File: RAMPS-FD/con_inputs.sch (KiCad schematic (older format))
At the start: 20 parts, among them K301 X-MIN, K302 X-MAX, K303 Y-MIN, K304 Y-MAX, K305 Z-MIN, K306 Z-MAX, P301 CONN_6, U301 74HC4050

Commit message: RAMPS-FD update
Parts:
- removed R304, R305, R306, R307, R308, R309: 10k, symbol R
- removed U301: 74HC4050, symbol 4050_RMC
- added C304, C305: 100n, symbol C
- added U301: TXS0108, symbol TXS0108
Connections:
- wire segments 76 -> 71
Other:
- moved on the sheet: K301, K302, K303, K304, K305, K306

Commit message: First version of RAMPS-FD, RIB
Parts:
- removed P301: CONN_6, symbol CONN_6
- added C501: 10u, symbol CP1
- added C502, C503, C504, C505: 100nF, symbol C
- added P301: CONN_4X2, symbol CONN_4X2
- added R501: 4k7, symbol R
- added R502, R503, R504, R505: 22, symbol R
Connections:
- net labels added: +V_LOGIC, THERM3, UART_RX, UART_RX_LVC, UART_TX, UART_TX_LVC
- net labels removed: +3.3V
- wire segments 71 -> 97
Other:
- note added: "From \nthermistor"
- note added: "Should use AREF?"
- note added: "To CPU"
- moved on the sheet: C301, C302, C303, R301, R302, R303

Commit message: RAMPS-FD update
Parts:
- removed C304: 100n, symbol C
- removed U301: TXS0108, symbol TXS0108
- added U4: 74LVC07A, symbol 74LVC07A
- C502, C503, C504, C505: value 100nF -> 100n
- R502, R503, R504, R505: value 22 -> 22R
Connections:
- net labels removed: UART_RX, UART_RX_LVC, UART_TX, UART_TX_LVC
- wire segments 97 -> 87

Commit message: Updates to RAMPS-FD
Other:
- note added: "Endstop inputs are 5V tolerant"
- note removed: "Endstops 5V"
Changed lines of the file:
@@
-EESchema Schematic File Version 2  date 19/09/2013 22:01:21
+EESchema Schematic File Version 2
 LIBS:power
 LIBS:device
@@
 LIBS:opendous
 LIBS:RAMPS-FD-cache
-EELAYER 25  0
+EELAYER 27 0
 EELAYER END
-$Descr A4 11700 8267
+$Descr A4 11693 8268
 encoding utf-8
-Sheet 8 8
+Sheet 8 9
 Title "RAMPS-FS RAMPS for Due"
-Date "19 sep 2013"
+Date "22 sep 2013"
 Rev "0.2"
 Comp ""
@@
 F 0 "U4" H 3950 3250 60  0000 C CNN
 F 1 "74LVC07A" H 4500 3250 60  0000 C CNN
+F 2 "" H 4200 3850 60  0001 C CNN
+F 3 "" H 4200 3850 60  0001 C CNN
 	1    4200 3850
 	1    0    0    -1
@@
 F 0 "R504" V 8800 1250 50  0000 C CNN
 F 1 "22R" V 8900 1250 50  0000 C CNN
+F 2 "" H 8900 1250 60  0001 C CNN
+F 3 "" H 8900 1250 60  0001 C CNN
 	1    8900 1250
 	0    -1   -1   0
@@
 F 0 "C504" H 9250 1600 50  0000 L CNN
 F 1 "100n" H 9250 1400 50  0000 L CNN
+F 2 "" H 9200 1500 60  0001 C CNN
+F 3 "" H 9200 1500 60  0001 C CNN
 	1    9200 1500
 	1    0    0    -1
@@
 F 0 "R505" V 8800 2750 50  0000 C CNN
 F 1 "22R" V 8900 2750 50  0000 C CNN
+F 2 "" H 8900 2750 60  0001 C CNN
+F 3 "" H 8900 2750 60  0001 C CNN
 	1    8900 2750
 	0    -1   -1   0
@@
 F 0 "C505" H 9250 3100 50  0000 L CNN
 F 1 "100n" H 9250 2900 50  0000 L CNN
+F 2 "" H 9200 3000 60  0001 C CNN
+F 3 "" H 9200 3000 60  0001 C CNN
 	1    9200 3000
 	1    0    0    -1
@@
 F 0 "C503" H 9050 4650 50  0000 L CNN
 F 1 "100n" H 9050 4450 50  0000 L CNN
+F 2 "" H 9000 4550 60  0001 C CNN
+F 3 "" H 9000 4550 60  0001 C CNN
 	1    9000 4550
 	1    0    0    -1
@@
 F 0 "R503" V 8600 4300 50  0000 C CNN
 F 1 "22R" V 8700 4300 50  0000 C CNN
+F 2 "" H 8700 4300 60  0001 C CNN
+F 3 "" H 8700 4300 60  0001 C CNN
 	1    8700 4300
 	0    -1   -1   0
@@
 F 0 "R502" V 8600 5850 50  0000 C CNN
 F 1 "22R" V 8700 5850 50  0000 C CNN
+F 2 "" H 8700 5850 60  0001 C CNN
+F 3 "" H 8700 5850 60  0001 C CNN
 	1    8700 5850
 	0    -1   -1   0
@@
 F 0 "C502" H 9050 6300 50  0000 L CNN
 F 1 "100n" H 9050 6100 50  0000 L CNN
+F 2 "" H 9000 6200 60  0001 C CNN
+F 3 "" H 9000 6200 60  0001 C CNN
 	1    9000 6200
 	1    0    0    -1
@@
 F 0 "#PWR098" H 9800 5170 30  0001 C CNN
 F 1 "+V_LOGIC" H 9800 5300 30  0000 C CNN
+F 2 "" H 9800 5200 60  0001 C CNN
+F 3 "" H 9800 5200 60  0001 C CNN
 	1    9800 5200
 	1    0    0    -1
@@
 F 0 "#PWR099" H 9800 3670 30  0001 C CNN
 F 1 "+V_LOGIC" H 9800 3800 30  0000 C CNN
+F 2 "" H 9800 3700 60  0001 C CNN
+F 3 "" H 9800 3700 60  0001 C CNN
 	1    9800 3700
 	1    0    0    -1
@@
 F 0 "#PWR0100" H 9800 2120 30  0001 C CNN
 F 1 "+V_LOGIC" H 9800 2250 30  0000 C CNN
+F 2 "" H 9800 2150 60  0001 C CNN
+F 3 "" H 9800 2150 60  0001 C CNN
 	1    9800 2150
 	1    0    0    -1
@@
 F 0 "#PWR0101" H 9800 620 30  0001 C CNN
 F 1 "+V_LOGIC" H 9800 750 30  0000 C CNN
+F 2 "" H 9800 650 60  0001 C CNN
+F 3 "" H 9800 650 60  0001 C CNN
 	1    9800 650
 	1    0    0    -1
@@
 F 0 "#PWR0102" H 4200 2920 30  0001 C CNN
 F 1 "+V_LOGIC" H 4200 3050 30  0000 C CNN
+F 2 "" H 4200 2950 60  0001 C CNN
+F 3 "" H 4200 2950 60  0001 C CNN
 	1    4200 2950
 	1    0    0    -1
@@
 F 0 "#PWR0103" H 4500 1670 30  0001 C CNN
 F 1 "+V_LOGIC" H 4500 1800 30  0000 C CNN
+F 2 "" H 4500 1700 60  0001 C CNN
+F 3 "" H 4500 1700 60  0001 C CNN
 	1    4500 1700
 	1    0    0    -1
@@
 F 0 "R501" V 9880 5550 50  0000 C CNN
 F 1 "4k7" V 9800 5550 50  0000 C CNN
+F 2 "" H 9800 5550 60  0001 C CNN
+F 3 "" H 9800 5550 60  0001 C CNN
 	1    9800 5550
 	1    0    0    -1
@@
 F 0 "C501" H 9850 6300 50  0000 L CNN
 F 1 "10u" H 9850 6100 50  0000 L CNN
+F 2 "" H 9800 6200 60  0001 C CNN
+F 3 "" H 9800 6200 60  0001 C CNN
 	1    9800 6200
 	1    0    0    -1
@@
 F 0 "#PWR0104" H 9800 6600 30  0001 C CNN
 F 1 "GND" H 9800 6530 30  0001 C CNN
+F 2 "" H 9800 6600 60  0001 C CNN
+F 3 "" H 9800 6600 60  0001 C CNN
 	1    9800 6600
 	1    0    0    -1
@@
 F 0 "#PWR0105" H 6250 2800 30  0001 C CNN
 F 1 "GND" H 6250 2730 30  0001 C CNN
+F 2 "" H 6250 2800 60  0001 C CNN
+F 3 "" H 6250 2800 60  0001 C CNN
 	1    6250 2800
 	1    0    0    -1
@@
 F 0 "P301" H 6850 2600 50  0000 C CNN
 F 1 "CONN_4X2" V 6850 2350 40  0000 C CNN
+F 2 "" H 6850 2350 60  0001 C CNN
+F 3 "" H 6850 2350 60  0001 C CNN
 	1    6850 2350
 	1    0    0    -1
@@
 F 0 "#PWR0106" H 4500 2300 30  0001 C CNN
 F 1 "GND" H 4500 2230 30  0001 C CNN
+F 2 "" H 4500 2300 60  0001 C CNN
+F 3 "" H 4500 2300 60  0001 C CNN
 	1    4500 2300
 	1    0    0    -1
@@
 F 0 "C305" H 4550 2100 50  0000 L CNN
 F 1 "100n" H 4550 1900 50  0000 L CNN
+F 2 "" H 4500 2000 60  0001 C CNN
+F 3 "" H 4500 2000 60  0001 C CNN
 	1    4500 2000
 	1    0    0    -1
@@
 F 0 "#PWR0107" H 1650 1590 20  0001 C CNN
 F 1 "+5V" H 1650 1590 30  0000 C CNN
+F 2 "" H 1650 1500 60  0001 C CNN
+F 3 "" H 1650 1500 60  0001 C CNN
 	1    1650 1500
 	1    0    0    -1
@@
 F 0 "#PWR0108" H 4200 4750 30  0001 C CNN
 F 1 "GND" H 4200 4680 30  0001 C CNN
+F 2 "" H 4200 4750 60  0001 C CNN
+F 3 "" H 4200 4750 60  0001 C CNN
 	1    4200 4750
 	1    0    0    -1
@@
 F 0 "#PWR0109" H 9800 4850 30  0001 C CNN
 F 1 "GND" H 9800 4780 30  0001 C CNN
+F 2 "" H 9800 4850 60  0001 C CNN
+F 3 "" H 9800 4850 60  0001 C CNN
 	1    9800 4850
 	1    0    0    -1
@@
 F 0 "C303" H 9850 4650 50  0000 L CNN
 F 1 "10u" H 9850 4450 50  0000 L CNN
+F 2 "" H 9800 4550 60  0001 C CNN
+F 3 "" H 9800 4550 60  0001 C CNN
 	1    9800 4550
 	1    0    0    -1
@@
 F 0 "R303" V 9880 4000 50  0000 C CNN
 F 1 "4k7" V 9800 4000 50  0000 C CNN
+F 2 "" H 9800 4000 60  0001 C CNN
+F 3 "" H 9800 4000 60  0001 C CNN
 	1    9800 4000
 	1    0    0    -1
@@
 F 0 "R302" V 9880 2450 50  0000 C CNN
 F 1 "4k7" V 9800 2450 50  0000 C CNN
+F 2 "" H 9800 2450 60  0001 C CNN
+F 3 "" H 9800 2450 60  0001 C CNN
 	1    9800 2450
 	1    0    0    -1
@@
 F 0 "C302" H 9850 3100 50  0000 L CNN
 F 1 "10u" H 9850 2900 50  0000 L CNN
+F 2 "" H 9800 3000 60  0001 C CNN
+F 3 "" H 9800 3000 60  0001 C CNN
 	1    9800 3000
 	1    0    0    -1
@@
 F 0 "#PWR0110" H 9800 3300 30  0001 C CNN
 F 1 "GND" H 9800 3230 30  0001 C CNN
+F 2 "" H 9800 3300 60  0001 C CNN
+F 3 "" H 9800 3300 60  0001 C CNN
 	1    9800 3300
 	1    0    0    -1
@@
 F 0 "#PWR0111" H 9800 1800 30  0001 C CNN
 F 1 "GND" H 9800 1730 30  0001 C CNN
+F 2 "" H 9800 1800 60  0001 C CNN
+F 3 "" H 9800 1800 60  0001 C CNN
 	1    9800 1800
 	1    0    0    -1
@@
 F 0 "C301" H 9850 1600 50  0000 L CNN
 F 1 "10u" H 9850 1400 50  0000 L CNN
+F 2 "" H 9800 1500 60  0001 C CNN
+F 3 "" H 9800 1500 60  0001 C CNN
 	1    9800 1500
 	1    0    0    -1
@@
 F 0 "R301" V 9880 950 50  0000 C CNN
 F 1 "4k7" V 9800 950 50  0000 C CNN
+F 2 "" H 9800 950 60  0001 C CNN
+F 3 "" H 9800 950 60  0001 C CNN
 	1    9800 950
 	1    0    0    -1
 $EndComp
-Text Notes 1350 2000 2    50   Italic 0
-Endstops 5V
+Text Notes 1850 2150 0    50   Italic 0
+Endstop inputs are 5V tolerant
 Text Notes 1600 6250 2    50   ~ 0
 Endstops
@@
 F 0 "#PWR0112" H 1850 5950 30  0001 C CNN
 F 1 "GND" H 1850 5880 30  0001 C CNN
+F 2 "" H 1850 5950 60  0001 C CNN
+F 3 "" H 1850 5950 60  0001 C CNN
 	1    1850 5950
 	1    0    0    -1
@@
 F 0 "K306" V 1100 2450 50  0000 C CNN
 F 1 "Z-MAX" V 1200 2450 40  0000 C CNN
+F 2 "" H 1150 2450 60  0001 C CNN
+F 3 "" H 1150 2450 60  0001 C CNN
 	1    1150 2450
 	-1   0    0    -1
@@
 F 0 "K305" V 1100 3150 50  0000 C CNN
 F 1 "Z-MIN" V 1200 3150 40  0000 C CNN
+F 2 "" H 1150 3150 60  0001 C CNN
+F 3 "" H 1150 3150 60  0001 C CNN
 	1    1150 3150
 	-1   0    0    -1
@@
 F 0 "K304" V 1100 3750 50  0000 C CNN
 F 1 "Y-MAX" V 1200 3750 40  0000 C CNN
+F 2 "" H 1150 3750 60  0001 C CNN
+F 3 "" H 1150 3750 60  0001 C CNN
 	1    1150 3750
 	-1   0    0    -1
@@
 F 0 "K303" V 1100 4350 50  0000 C CNN
 F 1 "Y-MIN" V 1200 4350 40  0000 C CNN
+F 2 "" H 1150 4350 60  0001 C CNN
+F 3 "" H 1150 4350 60  0001 C CNN
 	1    1150 4350
 	-1   0    0    -1
@@
 F 0 "K302" V 1100 4950 50  0000 C CNN
 F 1 "X-MAX" V 1200 4950 40  0000 C CNN
+F 2 "" H 1150 4950 60  0001 C CNN
+F 3 "" H 1150 4950 60  0001 C CNN
 	1    1150 4950
 	-1   0    0    -1
@@
 F 0 "K301" V 1100 5550 50  0000 C CNN
 F 1 "X-MIN" V 1200 5550 40  0000 C CNN
+F 2 "" H 1150 5550 60  0001 C CNN
+F 3 "" H 1150 5550 60  0001 C CNN
 	1    1150 5550
 	-1   0    0    -1

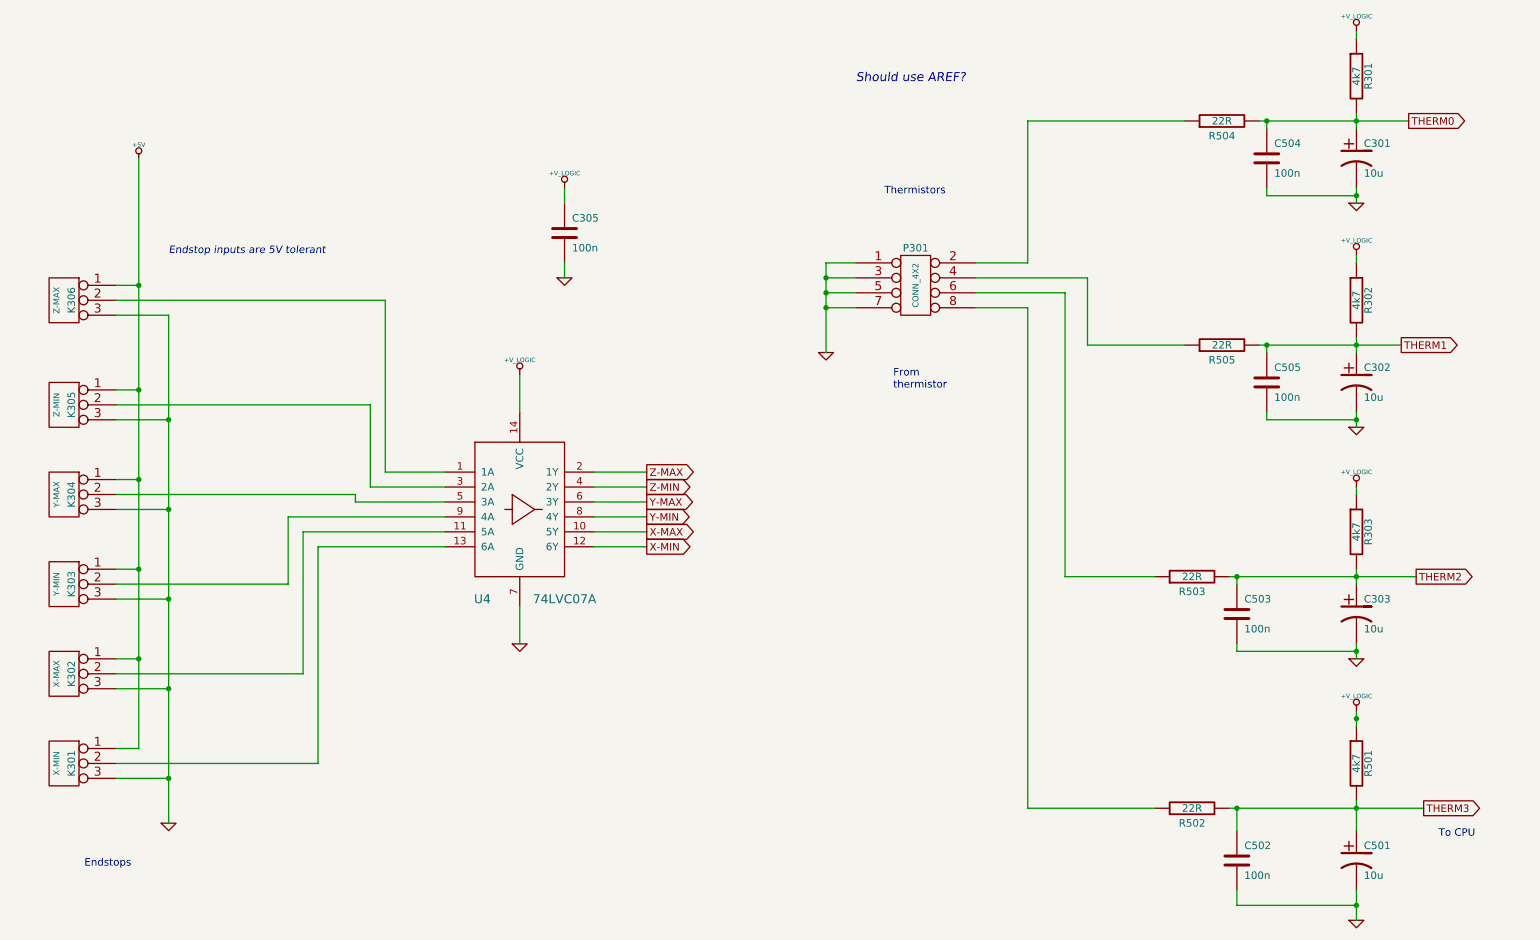
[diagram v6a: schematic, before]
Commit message: RAMPS-FD: update schematic, layout
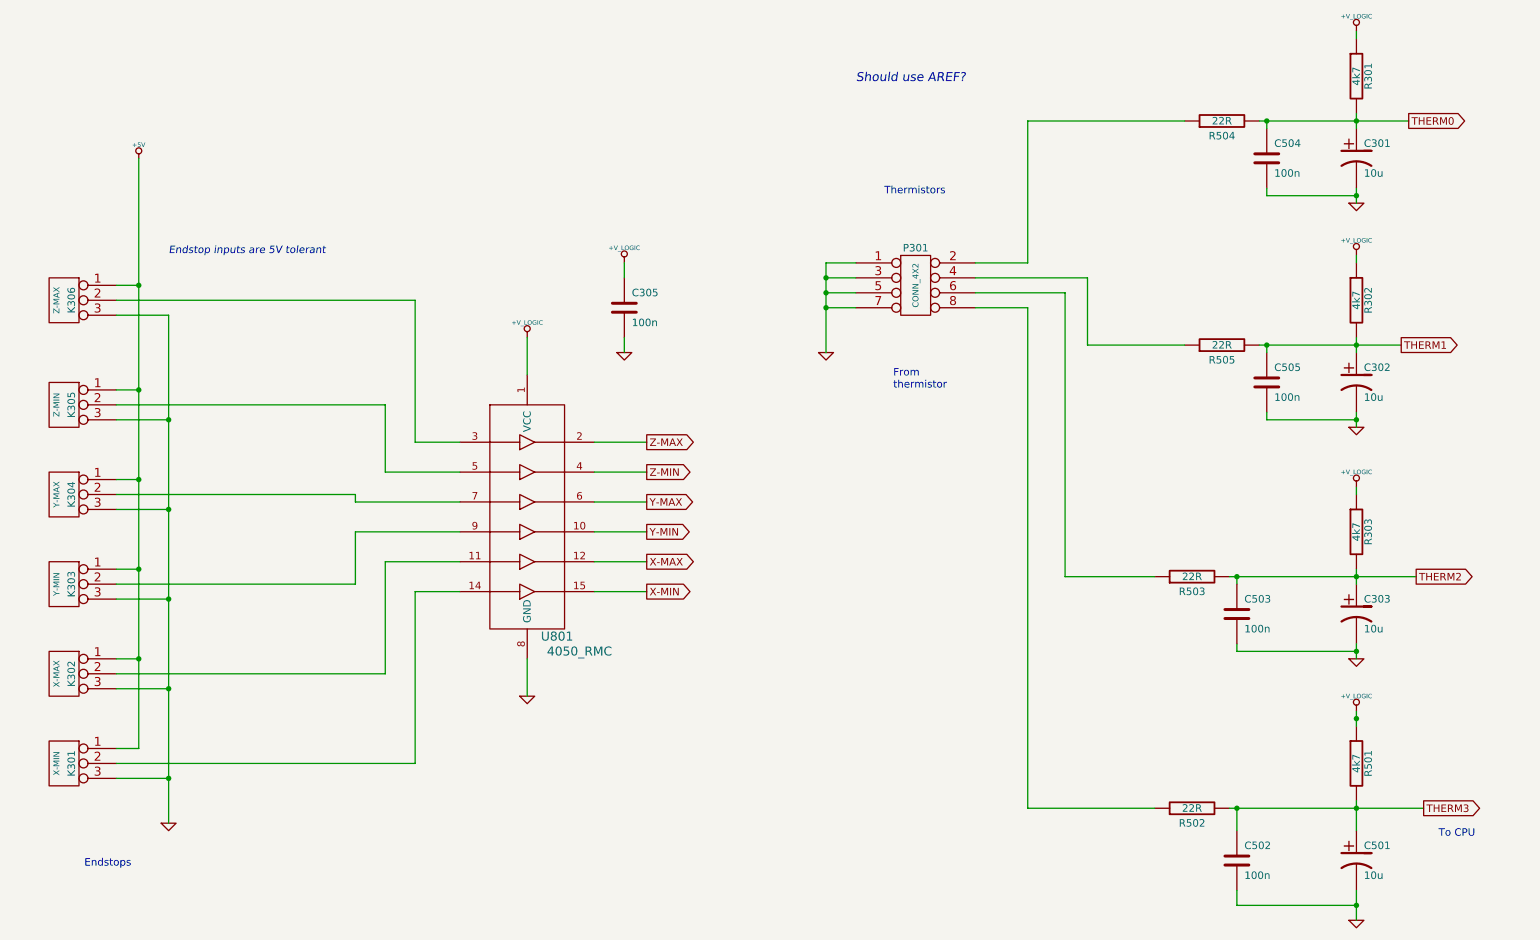
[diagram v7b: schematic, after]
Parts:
- removed U4: 74LVC07A, symbol 74LVC07A
- added U801: 4050_RMC, ~, symbol 4050_RMC
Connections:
- net +V_LOGIC: now also U801.1 (VCC)
- net GND: now also U801.8 (GND)
- net X-MAX: now also U801.12
- net X-MIN: now also U801.15
- net Y-MAX: now also U801.6
- net Y-MIN: now also U801.10
- net Z-MAX: now also U801.2
- net Z-MIN: now also U801.4
- net at K301.2 (PM): now also U801.14
- net at K302.2 (PM): now also U801.11
- net at K303.2 (PM): now also U801.9
- net at K304.2 (PM): now also U801.7
- net at K305.2 (PM): now also U801.5
- net at K306.2 (PM): now also U801.3
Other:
- moved on the sheet: C305
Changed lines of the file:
@@
 Sheet 8 9
 Title "RAMPS-FS RAMPS for Due"
-Date "24 sep 2013"
+Date "26 sep 2013"
 Rev "0.2"
 Comp ""
@@
 Comment4 ""
 $EndDescr
-$Comp
-L 74LVC07A U4
-U 1 1 523B4B0F
-P 4200 3850
-F 0 "U4" H 3950 3250 60  0000 C CNN
-F 1 "74LVC07A" H 4500 3250 60  0000 C CNN
-F 2 "" H 4200 3850 60  0001 C CNN
-F 3 "" H 4200 3850 60  0001 C CNN
-	1    4200 3850
-	1    0    0    -1
-$EndComp
 Connection ~ 1650 4850
 Wire Wire Line
@@
 Connection ~ 1850 3250
 Wire Wire Line
-	1850 5950 1850 2550
+	1850 2550 1850 5950
 Wire Wire Line
 	1850 2550 1500 2550
@@
 	1850 5050 1500 5050
 Wire Wire Line
-	2850 5550 2850 4100
-Wire Wire Line
-	2850 5550 1500 5550
-Wire Wire Line
-	2650 4350 2650 3900
-Wire Wire Line
-	2650 4350 1500 4350
-Wire Wire Line
-	1500 3150 3200 3150
+	3500 5550 3500 4400
+Wire Wire Line
+	3500 5550 1500 5550
+Wire Wire Line
+	3100 4350 3100 4000
+Wire Wire Line
+	3100 4350 1500 4350
+Wire Wire Line
+	1500 3150 3300 3150
 Wire Wire Line
 	7250 2400 7850 2400
@@
 Connection ~ 9800 6500
 Wire Wire Line
-	9800 6600 9800 6400
+	9800 6400 9800 6600
 Connection ~ 9800 5850
 Wire Wire Line
 	9800 5800 9800 6000
 Wire Wire Line
-	9800 5300 9800 5200
+	9800 5200 9800 5300
 Connection ~ 6250 2400
 Wire Wire Line
@@
 	6250 2500 6450 2500
 Wire Wire Line
-	4500 2300 4500 2200
-Wire Wire Line
-	2850 4100 3700 4100
-Wire Wire Line
-	2650 3900 3700 3900
-Wire Wire Line
-	3700 3700 3200 3700
+	4900 2800 4900 2700
+Wire Wire Line
+	3500 4400 3800 4400
+Wire Wire Line
+	3100 4000 3800 4000
+Wire Wire Line
+	3800 3600 3300 3600
 Wire Wire Line
 	3100 3800 3100 3750
 Wire Wire Line
-	5050 4000 4700 4000
+	5050 4200 4700 4200
 Wire Wire Line
 	5050 3800 4700 3800
 Wire Wire Line
-	4200 4750 4200 4500
-Wire Wire Line
-	5050 3600 4700 3600
+	4250 5100 4250 4850
+Wire Wire Line
+	5050 3400 4700 3400
 Wire Wire Line
 	9800 650  9800 700
 Wire Wire Line
-	9800 1300 9800 1200
+	9800 1200 9800 1300
 Connection ~ 9800 1250
 Wire Wire Line
-	9800 1800 9800 1700
-Wire Wire Line
-	9800 3300 9800 3200
+	9800 1700 9800 1800
+Wire Wire Line
+	9800 3200 9800 3300
 Connection ~ 9800 2750
 Wire Wire Line
-	9800 2800 9800 2700
+	9800 2700 9800 2800
 Wire Wire Line
 	9800 2150 9800 2200
@@
 	9800 3700 9800 3750
 Wire Wire Line
-	9800 4350 9800 4250
+	9800 4250 9800 4350
 Connection ~ 9800 4300
 Wire Wire Line
-	9800 4850 9800 4750
-Wire Wire Line
-	4200 3200 4200 2950
-Wire Wire Line
-	4700 3700 5050 3700
-Wire Wire Line
-	4700 3900 5050 3900
-Wire Wire Line
-	4700 4100 5050 4100
-Wire Wire Line
-	3200 3700 3200 3150
-Wire Wire Line
-	3700 3600 3300 3600
-Wire Wire Line
-	3300 3600 3300 2450
-Wire Wire Line
-	3100 3800 3700 3800
-Wire Wire Line
-	3700 4000 2750 4000
-Wire Wire Line
-	4500 1800 4500 1700
+	9800 4750 9800 4850
+Wire Wire Line
+	4250 2950 4250 2700
+Wire Wire Line
+	4700 3600 5050 3600
+Wire Wire Line
+	4700 4000 5050 4000
+Wire Wire Line
+	4700 4400 5050 4400
+Wire Wire Line
+	3300 3600 3300 3150
+Wire Wire Line
+	3800 3400 3500 3400
+Wire Wire Line
+	3500 3400 3500 2450
+Wire Wire Line
+	3100 3800 3800 3800
+Wire Wire Line
+	3800 4200 3300 4200
+Wire Wire Line
+	4900 2300 4900 2200
 Wire Wire Line
 	6250 2400 6450 2400
@@
 	8000 2750 8650 2750
 Wire Wire Line
-	3300 2450 1500 2450
+	3500 2450 1500 2450
 Wire Wire Line
 	3100 3750 1500 3750
 Wire Wire Line
-	2750 4000 2750 4950
-Wire Wire Line
-	2750 4950 1500 4950
+	3300 4200 3300 4950
+Wire Wire Line
+	3300 4950 1500 4950
 Wire Wire Line
 	1850 5650 1500 5650
@@
 L +V_LOGIC #PWR0103
 U 1 1 517866F1
-P 4200 2950
-F 0 "#PWR0103" H 4200 2920 30  0001 C CNN
-F 1 "+V_LOGIC" H 4200 3050 30  0000 C CNN
-F 2 "" H 4200 2950 60  0001 C CNN
-F 3 "" H 4200 2950 60  0001 C CNN
-	1    4200 2950
+P 4250 2700
+F 0 "#PWR0103" H 4250 2670 30  0001 C CNN
+F 1 "+V_LOGIC" H 4250 2800 30  0000 C CNN
+F 2 "" H 4250 2700 60  0001 C CNN
+F 3 "" H 4250 2700 60  0001 C CNN
+	1    4250 2700
 	1    0    0    -1
 $EndComp
@@
 L +V_LOGIC #PWR0104
 U 1 1 517866E5
-P 4500 1700
-F 0 "#PWR0104" H 4500 1670 30  0001 C CNN
-F 1 "+V_LOGIC" H 4500 1800 30  0000 C CNN
-F 2 "" H 4500 1700 60  0001 C CNN
-F 3 "" H 4500 1700 60  0001 C CNN
-	1    4500 1700
+P 4900 2200
+F 0 "#PWR0104" H 4900 2170 30  0001 C CNN
+F 1 "+V_LOGIC" H 4900 2300 30  0000 C CNN
+F 2 "" H 4900 2200 60  0001 C CNN
+F 3 "" H 4900 2200 60  0001 C CNN
+	1    4900 2200
 	1    0    0    -1
 $EndComp
@@
 L GND #PWR0107
 U 1 1 510D87E0
-P 4500 2300
-F 0 "#PWR0107" H 4500 2300 30  0001 C CNN
-F 1 "GND" H 4500 2230 30  0001 C CNN
-F 2 "" H 4500 2300 60  0001 C CNN
-F 3 "" H 4500 2300 60  0001 C CNN
-	1    4500 2300
+P 4900 2800
+F 0 "#PWR0107" H 4900 2800 30  0001 C CNN
+F 1 "GND" H 4900 2730 30  0001 C CNN
+F 2 "" H 4900 2800 60  0001 C CNN
+F 3 "" H 4900 2800 60  0001 C CNN
+	1    4900 2800
 	1    0    0    -1
 $EndComp
@@
 L C C305
 U 1 1 510D87AD
-P 4500 2000
-F 0 "C305" H 4550 2100 50  0000 L CNN
-F 1 "100n" H 4550 1900 50  0000 L CNN
-F 2 "" H 4500 2000 60  0001 C CNN
-F 3 "" H 4500 2000 60  0001 C CNN
-	1    4500 2000
+P 4900 2500
+F 0 "C305" H 4950 2600 50  0000 L CNN
+F 1 "100n" H 4950 2400 50  0000 L CNN
+F 2 "" H 4900 2500 60  0001 C CNN
+F 3 "" H 4900 2500 60  0001 C CNN
+	1    4900 2500
 	1    0    0    -1
 $EndComp
@@
 L GND #PWR0109
 U 1 1 50FF1A09
-P 4200 4750
-F 0 "#PWR0109" H 4200 4750 30  0001 C CNN
-F 1 "GND" H 4200 4680 30  0001 C CNN
-F 2 "" H 4200 4750 60  0001 C CNN
-F 3 "" H 4200 4750 60  0001 C CNN
-	1    4200 4750
+P 4250 5100
+F 0 "#PWR0109" H 4250 5100 30  0001 C CNN
+F 1 "GND" H 4250 5030 30  0001 C CNN
+F 2 "" H 4250 5100 60  0001 C CNN
+F 3 "" H 4250 5100 60  0001 C CNN
+	1    4250 5100
 	1    0    0    -1
 $EndComp
@@
 Text Notes 1600 6250 2    50   ~ 0
 Endstops
+Text GLabel 5050 3400 2    50   Output ~ 0
+Z-MAX
 Text GLabel 5050 3600 2    50   Output ~ 0
-Z-MAX
-Text GLabel 5050 3700 2    50   Output ~ 0
 Z-MIN
-Text GLabel 5050 3900 2    50   Output ~ 0
+Text GLabel 5050 4000 2    50   Output ~ 0
 Y-MIN
 Text GLabel 5050 3800 2    50   Output ~ 0
 Y-MAX
-Text GLabel 5050 4000 2    50   Output ~ 0
+Text GLabel 5050 4200 2    50   Output ~ 0
 X-MAX
-Text GLabel 5050 4100 2    50   Output ~ 0
+Text GLabel 5050 4400 2    50   Output ~ 0
 X-MIN
 $Comp
@@
 	-1   0    0    -1
 $EndComp
+$Comp
+L 4050_RMC U801
+U 1 1 5244B8CC
+P 4450 3150
+F 0 "U801" H 4450 1600 60  0000 C CNN
+F 1 "4050_RMC" H 4600 1500 60  0000 C CNN
+F 2 "~" H 4450 3150 60  0000 C CNN
+F 3 "~" H 4450 3150 60  0000 C CNN
+	1    4450 3150
+	1    0    0    -1
+$EndComp
 $EndSCHEMATC
